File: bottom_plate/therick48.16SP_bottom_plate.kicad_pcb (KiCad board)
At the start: 2 copper layers, 313.9 x 76 mm, 89 parts, among them U1 HOLE, U10 HOLE, U11 HOLE, U12 HOLE, U13 HOLE, U14 HOLE, U15 HOLE, U16 HOLE, U17 HOLE, U18 HOLE, U19 HOLE, U2 HOLE, U20 HOLE, U21 HOLE, U22 HOLE, U23 HOLE, U24 HOLE, U25 HOLE, U26 HOLE, U27 HOLE, U28 HOLE, U29 HOLE, U3 HOLE, U30 HOLE, U31 HOLE, U32 HOLE, U33 HOLE, U34 HOLE, U35 HOLE, U36 HOLE, U37 HOLE, U38 HOLE, U39 HOLE, U4 HOLE, U40 HOLE, U41 HOLE, U42 HOLE, U43 HOLE, U44 HOLE, U45 HOLE, U46 HOLE, U47 HOLE, U48 HOLE, U49 HOLE, U5 HOLE, U50 HOLE, U51 HOLE, U52 HOLE, U53 HOLE, U54 HOLE, U55 HOLE, U56 HOLE, U57 HOLE, U58 HOLE, U59 HOLE, U6 HOLE, U60 HOLE, U61 HOLE, U62 HOLE, U63 HOLE, U64 HOLE, U65 HOLE, U66 HOLE, U67 HOLE, U68 HOLE, U69 HOLE, U7 HOLE, U70 HOLE, U8 HOLE, U9 HOLE

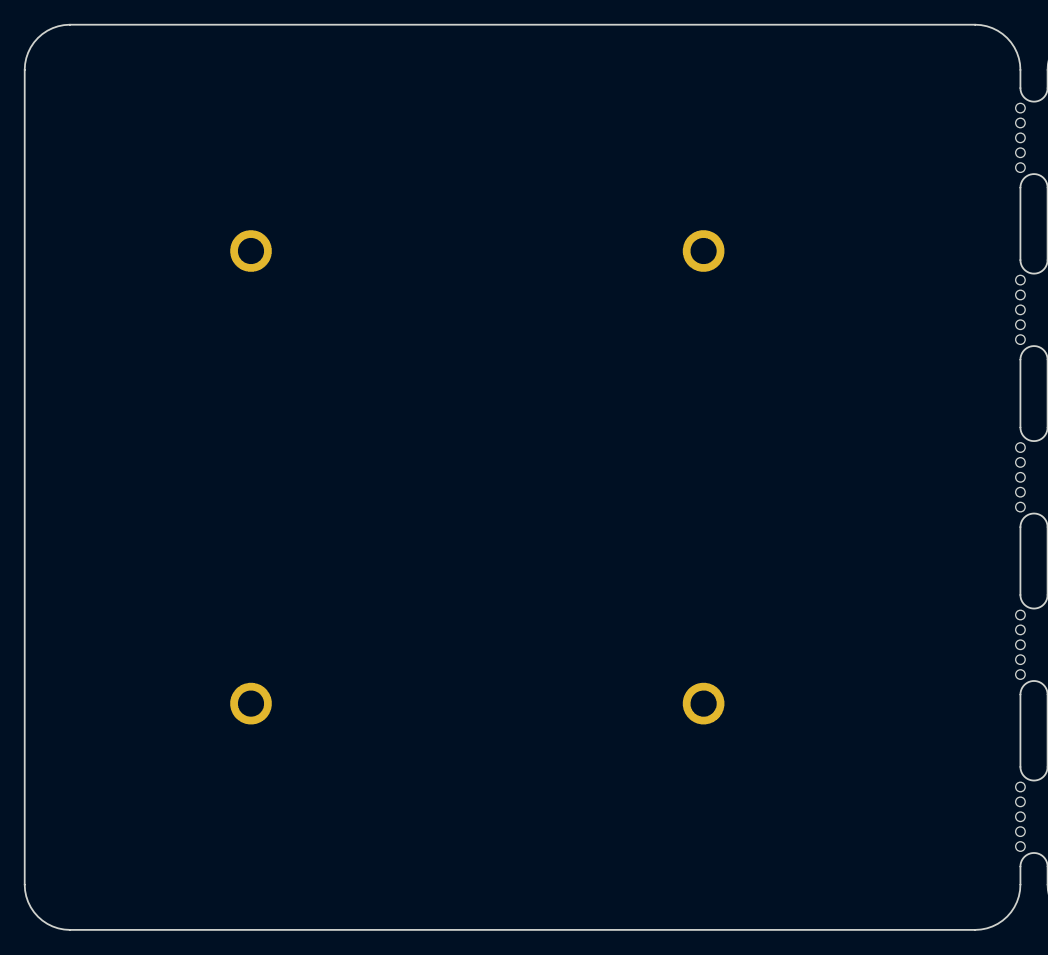
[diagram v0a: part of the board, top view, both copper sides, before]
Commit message: Changed gap between 4X12 and 4X4 to .25 inches
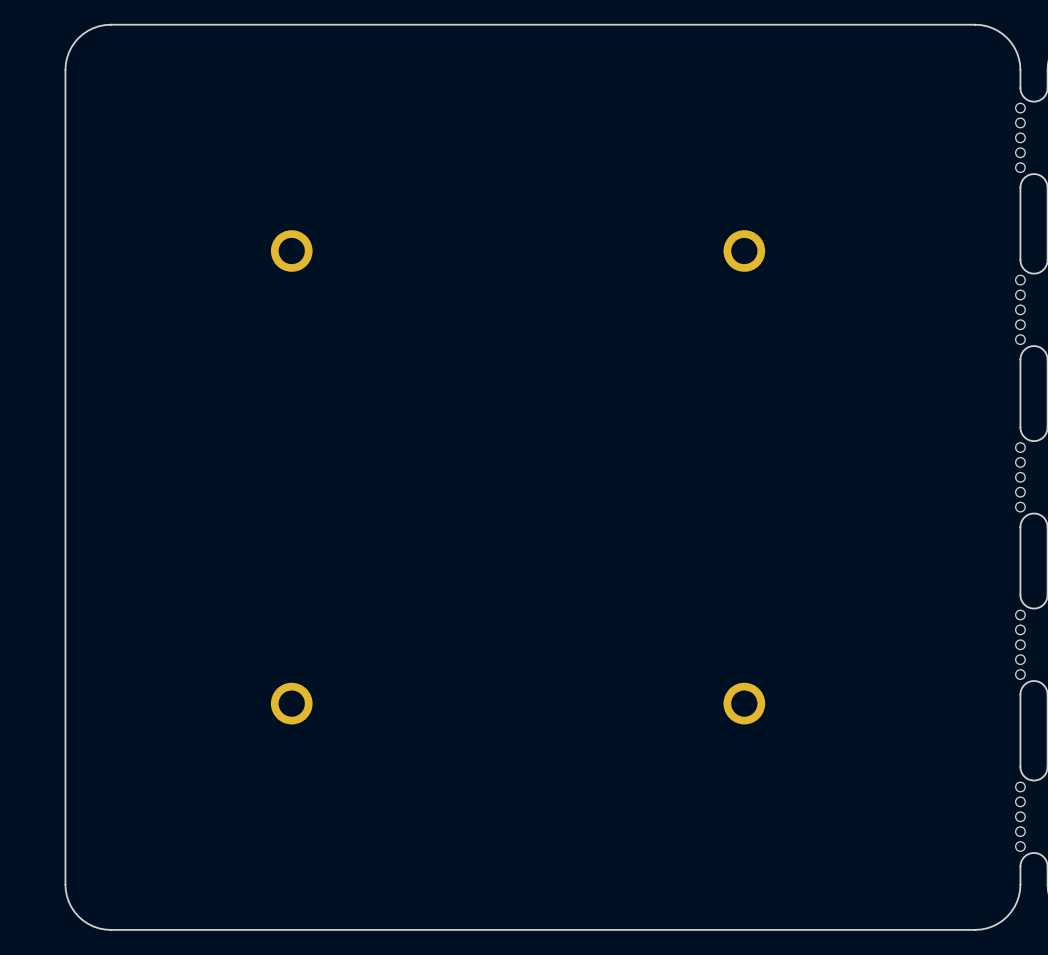
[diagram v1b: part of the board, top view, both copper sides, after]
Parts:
- moved H10 3.42 mm to (120.5, 59.7)
- moved H7 3.42 mm to (82.5, 59.7)
- moved H8 3.42 mm to (82.5, 97.7)
- moved H9 3.42 mm to (120.5, 97.7)
- moved U49 3.42 mm to (73.0, 50.2)
- moved U50 3.42 mm to (92.0, 50.2)
- moved U51 3.42 mm to (111.0, 50.2)
- moved U52 3.42 mm to (130.0, 50.2)
- moved U53 3.42 mm to (73.0, 69.2)
- moved U54 3.42 mm to (92.0, 69.2)
- moved U55 3.42 mm to (111.0, 69.2)
- moved U56 3.42 mm to (130.0, 69.2)
- moved U57 3.42 mm to (73.0, 88.2)
- moved U58 3.42 mm to (92.0, 88.2)
- moved U59 3.42 mm to (111.0, 88.2)
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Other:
- board size 313.9 x 76 mm -> 310.5 x 76 mm

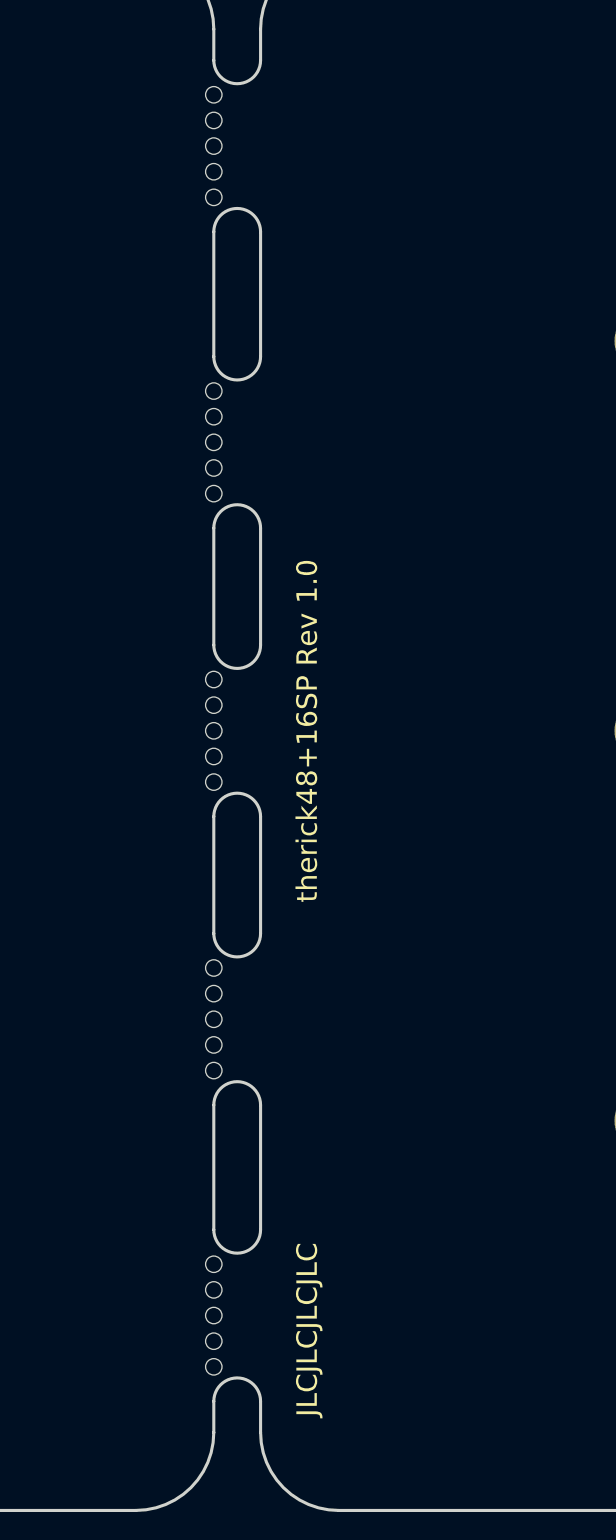
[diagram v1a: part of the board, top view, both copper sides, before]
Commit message: 48+16SP to 48.16SP
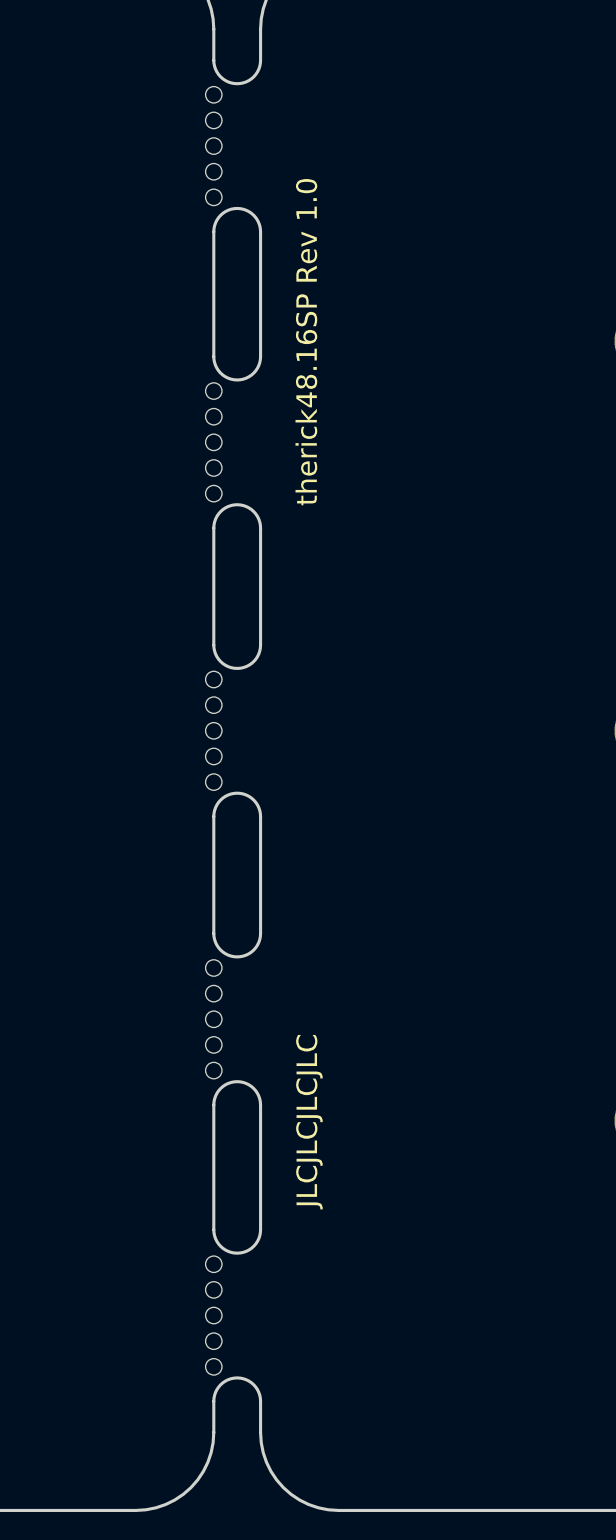
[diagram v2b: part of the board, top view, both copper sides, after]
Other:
- board text added: "therick48.16SP Rev 1.0"
- board text removed: "therick48+16SP Rev 1.0"
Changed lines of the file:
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@@
   (gr_arc (start 67.259991 44.46) (end 67.259991 40.66) (angle -90) (layer Edge.Cuts) (width 0.15))
   (gr_line (start 63.459991 112.86) (end 63.459991 44.46) (layer Edge.Cuts) (width 0.15))
-  (gr_text "therick48+16SP Rev 1.0" (at 148.19961 78.659793 90) (layer F.SilkS)
+  (gr_text "therick48.16SP Rev 1.0" (at 148.19961 59.69 90) (layer F.SilkS)
     (effects (font (size 1 1) (thickness 0.15)))
   )
@@
   (gr_arc (start 149.72 112.86) (end 145.92 112.86) (angle -90) (layer Edge.Cuts) (width 0.15))
   (gr_arc (start 149.72 44.46) (end 149.72 40.66) (angle -90) (layer Edge.Cuts) (width 0.15))
-  (gr_text JLCJLCJLCJLC (at 148.2 112.1 90) (layer F.SilkS)
-    (effects (font (size 1 1) (thickness 0.15)) (justify left))
+  (gr_text JLCJLCJLCJLC (at 148.209 97.663 90) (layer F.SilkS)
+    (effects (font (size 1 1) (thickness 0.15)))
   )
   (gr_line (start 317.0475 95.39375) (end 317.0475 100.15625) (layer Dwgs.User) (width 0.15))
